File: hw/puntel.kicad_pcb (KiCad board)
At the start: 2 copper layers, 101.6 x 20.3 mm, 49 parts, among them J1 UEXT, J2 STRIP-3, J3 USB-power, J4 USB-prog, J5 STRIP-4, J6 STRIP-4, Q1 DTA114, SW1 BUTTON, SW2 BUTTON, U1 AP2111H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

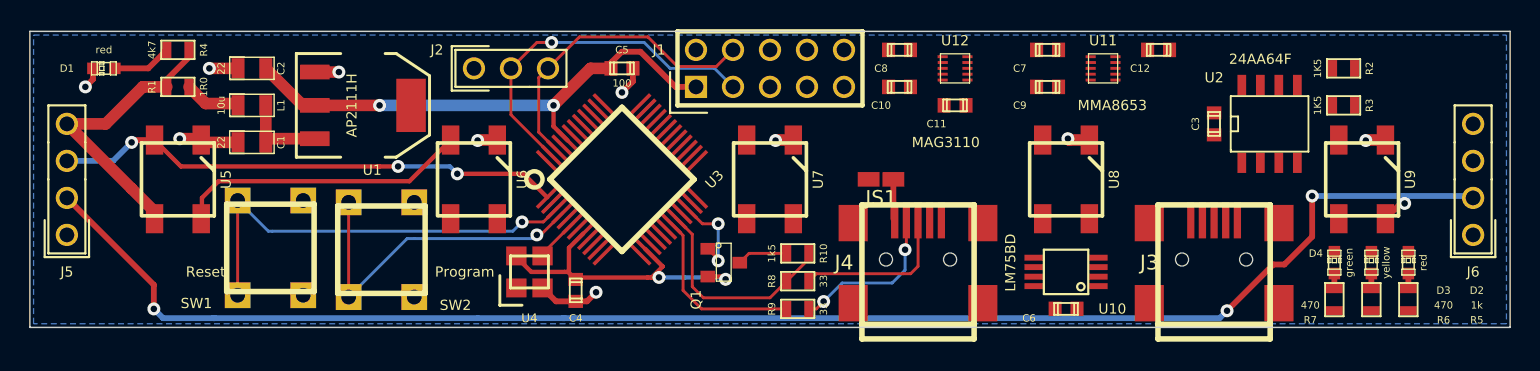
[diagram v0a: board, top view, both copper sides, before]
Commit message: hw: routed (without uext)
Signed-off-by: Alessandro Rubini <rubini@gnudd.com>
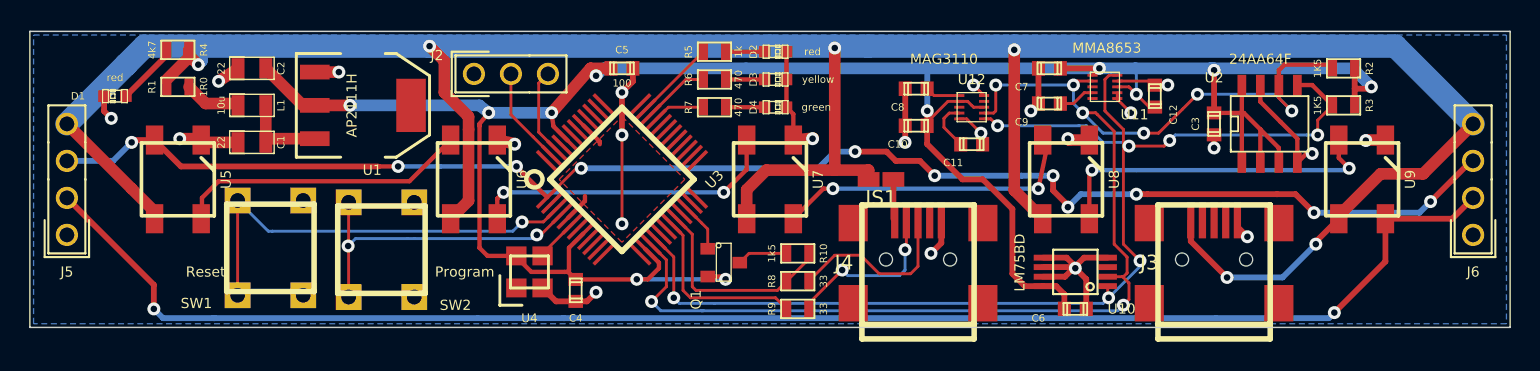
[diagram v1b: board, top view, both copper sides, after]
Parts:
- removed J1: UEXT, flat10
- moved R5 50.6 mm to (163.8, 77.6), turned to 0 degrees
- moved R6 47.6 mm to (163.8, 79.5), turned to 0 degrees
- moved D2 45.8 mm to (168.0, 77.6), turned to 0 degrees
- moved R7 44.5 mm to (163.8, 81.4), turned to 0 degrees
- moved D3 42.8 mm to (168.0, 79.5), turned to 0 degrees
- moved D4 39.8 mm to (168.0, 81.4), turned to 0 degrees
- moved C12 3.19 mm to (194.1, 80.6), turned to 270 degrees
- moved C10 2.90 mm to (177.7, 82.7)
- moved C11 2.90 mm to (181.5, 83.9)
- moved C8 2.90 mm to (177.7, 80.1)
- moved U12 2.90 mm to (181.5, 81.4)
- moved D1 2.05 mm to (122.7, 80.6)
- moved U11 1.28 mm to (190.6, 80.0)
- moved C7 1.28 mm to (186.8, 78.7)
- moved C9 1.15 mm to (186.8, 81.2)
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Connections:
- U12 pad 6: (no net) -> /SDA
- U3 pad 2: /SSEL -> (no net)
- U3 pad 24: /YLED -> (no net)
- U3 pad 27: /MISO -> (no net)
- U3 pad 28: /MOSI -> (no net)
- U3 pad 29: /SCK -> (no net)
- U3 pad 33: (no net) -> /GLED
- U3 pad 34: /RLED -> /YLED
- U3 pad 35: /GLED -> /RLED
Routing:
- net +5V: track 20.1 -> 188.4 mm, vias 0 -> 6
- net +3.3V: track 58.6 -> 178.6 mm, vias 4 -> 11
- net /SCL: track 0.00 -> 89.5 mm, vias 0 -> 8
- net /SDA: track 0.00 -> 83.5 mm, vias 0 -> 7
- net /Din: track 35.3 -> 104.8 mm, vias 3 -> 11
- net GND: track 21.0 -> 81.7 mm, vias 10 -> 23
- net N-0000045: track 0.00 -> 23.3 mm, vias 0 -> 2
- net N-0000064: track 0.00 -> 21.3 mm, vias 0 -> 2
- net N-0000046: track 0.00 -> 21.2 mm, vias 0 -> 2
- net /TXD: track 24.4 -> 6.83 mm, vias 1 -> 0
- net /RXD: track 21.4 -> 6.09 mm
- net /RLED: track 0.00 -> 5.65 mm
- net /YLED: track 0.00 -> 4.65 mm
- net /GLED: track 0.00 -> 3.66 mm
- net N-0000027: track 0.00 -> 3.46 mm
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- added copper zone on F.Cu, net GND
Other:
- net class Default: clearance 0.2 -> 0.19
- rule trace_clearance: 0.2 -> 0.19
